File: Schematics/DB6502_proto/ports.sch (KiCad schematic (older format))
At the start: 29 parts, among them J1 System Bus, J10 AVR-ISP-6, J2 Controls, J3 Debug UART, J4 I/O Bus, J5 USB_B, J6 Power, J7 Power, J8 Power, J9 Power, U9 FT230XS

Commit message: Initial PCB layout
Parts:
- removed J6, J7, J8, J9: Power, symbol Connector:Conn_01x02_Female
- C13, C14, C15, C16: footprint (none) -> Capacitor_THT:C_Disc_D5.0mm_W2.5mm_P2.50mm
- D1, D2: footprint (none) -> LED_THT:LED_D3.0mm
- FB1, R1, R10, R11, R2, R3, R4, R5, R6, R7, R8, R9: footprint (none) -> Resistor_THT:R_Axial_DIN0207_L6.3mm_D2.5mm_P10.16mm_Horizontal
- J1, J2, J4: footprint (none) -> Connector_PinSocket_2.54mm:PinSocket_1x32_P2.54mm_Vertical
- J10: footprint (none) -> Connector_PinSocket_2.54mm:PinSocket_2x03_P2.54mm_Vertical
- J3: footprint (none) -> Connector_PinHeader_2.54mm:PinHeader_1x06_P2.54mm_Horizontal
- J5: footprint (none) -> Connector_USB:USB_B_OST_USB-B1HSxx_Horizontal
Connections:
- wire segments 231 -> 223
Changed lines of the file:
@@
 F 0 "J1" H 4728 6176 50  0000 L CNN
 F 1 "System Bus" H 4728 6085 50  0000 L CNN
-F 2 "" H 4700 6200 50  0001 C CNN
+F 2 "Connector_PinSocket_2.54mm:PinSocket_1x32_P2.54mm_Vertical" H 4700 6200 50  0001 C CNN
 F 3 "~" H 4700 6200 50  0001 C CNN
 	1    4700 6200
@@
 F 0 "R6" H 2230 1154 50  0000 R CNN
 F 1 "4K7" H 2230 1245 50  0000 R CNN
-F 2 "" V 2230 1200 50  0001 C CNN
+F 2 "Resistor_THT:R_Axial_DIN0207_L6.3mm_D2.5mm_P10.16mm_Horizontal" V 2230 1200 50  0001 C CNN
 F 3 "~" H 2300 1200 50  0001 C CNN
 	1    2300 1200
@@
 F 0 "R5" H 2070 1246 50  0000 L CNN
 F 1 "4K7" H 2070 1155 50  0000 L CNN
-F 2 "" V 1930 1200 50  0001 C CNN
+F 2 "Resistor_THT:R_Axial_DIN0207_L6.3mm_D2.5mm_P10.16mm_Horizontal" V 1930 1200 50  0001 C CNN
 F 3 "~" H 2000 1200 50  0001 C CNN
 	1    2000 1200
@@
 F 0 "R4" H 1770 1246 50  0000 L CNN
 F 1 "4K7" H 1770 1155 50  0000 L CNN
-F 2 "" V 1630 1200 50  0001 C CNN
+F 2 "Resistor_THT:R_Axial_DIN0207_L6.3mm_D2.5mm_P10.16mm_Horizontal" V 1630 1200 50  0001 C CNN
 F 3 "~" H 1700 1200 50  0001 C CNN
 	1    1700 1200
@@
 F 0 "R3" H 1470 1246 50  0000 L CNN
 F 1 "4K7" H 1470 1155 50  0000 L CNN
-F 2 "" V 1330 1200 50  0001 C CNN
+F 2 "Resistor_THT:R_Axial_DIN0207_L6.3mm_D2.5mm_P10.16mm_Horizontal" V 1330 1200 50  0001 C CNN
 F 3 "~" H 1400 1200 50  0001 C CNN
 	1    1400 1200
@@
 F 0 "R2" H 1170 1246 50  0000 L CNN
 F 1 "4K7" H 1170 1155 50  0000 L CNN
-F 2 "" V 1030 1200 50  0001 C CNN
+F 2 "Resistor_THT:R_Axial_DIN0207_L6.3mm_D2.5mm_P10.16mm_Horizontal" V 1030 1200 50  0001 C CNN
 F 3 "~" H 1100 1200 50  0001 C CNN
 	1    1100 1200
@@
 F 0 "J2" H 5178 2626 50  0000 L CNN
 F 1 "Controls" H 5178 2535 50  0000 L CNN
-F 2 "" H 5150 2650 50  0001 C CNN
+F 2 "Connector_PinSocket_2.54mm:PinSocket_1x32_P2.54mm_Vertical" H 5150 2650 50  0001 C CNN
 F 3 "~" H 5150 2650 50  0001 C CNN
 	1    5150 2650
@@
 F 0 "R1" H 870 1246 50  0000 L CNN
 F 1 "4K7" H 870 1155 50  0000 L CNN
-F 2 "" V 730 1200 50  0001 C CNN
+F 2 "Resistor_THT:R_Axial_DIN0207_L6.3mm_D2.5mm_P10.16mm_Horizontal" V 730 1200 50  0001 C CNN
 F 3 "~" H 800 1200 50  0001 C CNN
 	1    800  1200
@@
 F 0 "J4" H 8128 2576 50  0000 L CNN
 F 1 "I/O Bus" H 8128 2485 50  0000 L CNN
-F 2 "" H 8100 2600 50  0001 C CNN
+F 2 "Connector_PinSocket_2.54mm:PinSocket_1x32_P2.54mm_Vertical" H 8100 2600 50  0001 C CNN
 F 3 "~" H 8100 2600 50  0001 C CNN
 	1    8100 2600
@@
 F 0 "J10" H 10021 1696 50  0000 R CNN
 F 1 "AVR-ISP-6" H 10021 1605 50  0000 R CNN
-F 2 "" V 10100 1650 50  0001 C CNN
+F 2 "Connector_PinSocket_2.54mm:PinSocket_2x03_P2.54mm_Vertical" V 10100 1650 50  0001 C CNN
 F 3 " ~" H 9075 1050 50  0001 C CNN
 	1    10350 1600
@@
 F 0 "J5" H 9007 3467 50  0000 C CNN
 F 1 "USB_B" H 9007 3376 50  0000 C CNN
-F 2 "" H 9100 2950 50  0001 C CNN
+F 2 "Connector_USB:USB_B_OST_USB-B1HSxx_Horizontal" H 9100 2950 50  0001 C CNN
 F 3 "" H 9100 2950 50  0001 C CNN
 	1    8950 3000
@@
 F 0 "FB1" V 9563 2800 50  0000 C CNN
 F 1 "FB" V 9654 2800 50  0000 C CNN
-F 2 "" V 9730 2800 50  0001 C CNN
+F 2 "Resistor_THT:R_Axial_DIN0207_L6.3mm_D2.5mm_P10.16mm_Horizontal" V 9730 2800 50  0001 C CNN
 F 3 "~" H 9800 2800 50  0001 C CNN
 	1    9800 2800
@@
 F 0 "C15" H 9965 5496 50  0000 L CNN
 F 1 "100nF" H 9965 5405 50  0000 L CNN
-F 2 "" H 9888 5300 50  0001 C CNN
+F 2 "Capacitor_THT:C_Disc_D5.0mm_W2.5mm_P2.50mm" H 9888 5300 50  0001 C CNN
 F 3 "~" H 9850 5450 50  0001 C CNN
 	1    9850 5450
@@
 F 0 "R8" H 10370 5496 50  0000 L CNN
 F 1 "220" H 10370 5405 50  0000 L CNN
-F 2 "" V 10230 5450 50  0001 C CNN
+F 2 "Resistor_THT:R_Axial_DIN0207_L6.3mm_D2.5mm_P10.16mm_Horizontal" V 10230 5450 50  0001 C CNN
 F 3 "~" H 10300 5450 50  0001 C CNN
 	1    10300 5450
@@
 F 0 "R11" H 10670 5496 50  0000 L CNN
 F 1 "220" H 10670 5405 50  0000 L CNN
-F 2 "" V 10530 5450 50  0001 C CNN
+F 2 "Resistor_THT:R_Axial_DIN0207_L6.3mm_D2.5mm_P10.16mm_Horizontal" V 10530 5450 50  0001 C CNN
 F 3 "~" H 10600 5450 50  0001 C CNN
 	1    10600 5450
@@
 F 0 "D1" V 10339 5733 50  0000 R CNN
 F 1 "RX" V 10248 5733 50  0000 R CNN
-F 2 "" H 10300 5850 50  0001 C CNN
+F 2 "LED_THT:LED_D3.0mm" H 10300 5850 50  0001 C CNN
 F 3 "~" H 10300 5850 50  0001 C CNN
 	1    10300 5850
@@
 F 0 "D2" V 10639 5732 50  0000 R CNN
 F 1 "TX" V 10548 5732 50  0000 R CNN
-F 2 "" H 10600 5850 50  0001 C CNN
+F 2 "LED_THT:LED_D3.0mm" H 10600 5850 50  0001 C CNN
 F 3 "~" H 10600 5850 50  0001 C CNN
 	1    10600 5850
@@
 Wire Wire Line
 	6050 3300 7900 3300
-$Comp
-L Connector:Conn_01x02_Female J6
-U 1 1 6034CE9D
-P 9250 5400
-F 0 "J6" H 9278 5376 50  0000 L CNN
-F 1 "Power" H 9278 5285 50  0000 L CNN
-F 2 "" H 9250 5400 50  0001 C CNN
-F 3 "~" H 9250 5400 50  0001 C CNN
-	1    9250 5400
-	1    0    0    -1
-$EndComp
-Text GLabel 8950 5400 0    50   Input ~ 0
-+5V
-Text GLabel 8950 5500 0    50   Input ~ 0
-GND
-Wire Wire Line
-	8950 5400 9050 5400
-Wire Wire Line
-	8950 5500 9050 5500
-$Comp
-L Connector:Conn_01x02_Female J7
-U 1 1 60363BED
-P 9250 5650
-F 0 "J7" H 9278 5626 50  0000 L CNN
-F 1 "Power" H 9278 5535 50  0000 L CNN
-F 2 "" H 9250 5650 50  0001 C CNN
-F 3 "~" H 9250 5650 50  0001 C CNN
-	1    9250 5650
-	1    0    0    -1
-$EndComp
-Text GLabel 8950 5650 0    50   Input ~ 0
-+5V
-Text GLabel 8950 5750 0    50   Input ~ 0
-GND
-Wire Wire Line
-	8950 5650 9050 5650
-Wire Wire Line
-	8950 5750 9050 5750
-$Comp
-L Connector:Conn_01x02_Female J8
-U 1 1 6036B691
-P 9250 5900
-F 0 "J8" H 9278 5876 50  0000 L CNN
-F 1 "Power" H 9278 5785 50  0000 L CNN
-F 2 "" H 9250 5900 50  0001 C CNN
-F 3 "~" H 9250 5900 50  0001 C CNN
-	1    9250 5900
-	1    0    0    -1
-$EndComp
-Text GLabel 8950 5900 0    50   Input ~ 0
-+5V
-Text GLabel 8950 6000 0    50   Input ~ 0
-GND
-Wire Wire Line
-	8950 5900 9050 5900
-Wire Wire Line
-	8950 6000 9050 6000
-$Comp
-L Connector:Conn_01x02_Female J9
-U 1 1 6036B69F
-P 9250 6150
-F 0 "J9" H 9278 6126 50  0000 L CNN
-F 1 "Power" H 9278 6035 50  0000 L CNN
-F 2 "" H 9250 6150 50  0001 C CNN
-F 3 "~" H 9250 6150 50  0001 C CNN
-	1    9250 6150
-	1    0    0    -1
-$EndComp
-Text GLabel 8950 6150 0    50   Input ~ 0
-+5V
-Text GLabel 8950 6250 0    50   Input ~ 0
-GND
-Wire Wire Line
-	8950 6150 9050 6150
-Wire Wire Line
-	8950 6250 9050 6250
 Text GLabel 10750 3000 2    50   BiDi ~ 0
 USBD-
@@
 F 0 "R10" V 10600 3250 50  0000 C CNN
 F 1 "27" V 10500 3250 50  0000 C CNN
-F 2 "" V 10430 3250 50  0001 C CNN
+F 2 "Resistor_THT:R_Axial_DIN0207_L6.3mm_D2.5mm_P10.16mm_Horizontal" V 10430 3250 50  0001 C CNN
 F 3 "~" H 10500 3250 50  0001 C CNN
 	1    10500 3250
@@
 F 0 "R9" V 10600 3000 50  0000 C CNN
 F 1 "27" V 10500 3000 50  0000 C CNN
-F 2 "" V 10430 3000 50  0001 C CNN
+F 2 "Resistor_THT:R_Axial_DIN0207_L6.3mm_D2.5mm_P10.16mm_Horizontal" V 10430 3000 50  0001 C CNN
 F 3 "~" H 10500 3000 50  0001 C CNN
 	1    10500 3000
@@
 F 0 "C14" H 9892 3496 50  0000 L CNN
 F 1 "47pF" H 9892 3405 50  0000 L CNN
-F 2 "" H 9800 3450 50  0001 C CNN
+F 2 "Capacitor_THT:C_Disc_D5.0mm_W2.5mm_P2.50mm" H 9800 3450 50  0001 C CNN
 F 3 "~" H 9800 3450 50  0001 C CNN
 	1    9800 3450
@@
 F 0 "C16" H 10242 3496 50  0000 L CNN
 F 1 "47pF" H 10242 3405 50  0000 L CNN
-F 2 "" H 10150 3450 50  0001 C CNN
+F 2 "Capacitor_THT:C_Disc_D5.0mm_W2.5mm_P2.50mm" H 10150 3450 50  0001 C CNN
 F 3 "~" H 10150 3450 50  0001 C CNN
 	1    10150 3450
@@
 F 0 "C13" H 9542 3496 50  0000 L CNN
 F 1 "10nF" H 9542 3405 50  0000 L CNN
-F 2 "" H 9450 3450 50  0001 C CNN
+F 2 "Capacitor_THT:C_Disc_D5.0mm_W2.5mm_P2.50mm" H 9450 3450 50  0001 C CNN
 F 3 "~" H 9450 3450 50  0001 C CNN
 	1    9450 3450
@@
 F 0 "R7" H 2230 2554 50  0000 R CNN
 F 1 "4K7" H 2230 2645 50  0000 R CNN
-F 2 "" V 2230 2600 50  0001 C CNN
+F 2 "Resistor_THT:R_Axial_DIN0207_L6.3mm_D2.5mm_P10.16mm_Horizontal" V 2230 2600 50  0001 C CNN
 F 3 "~" H 2300 2600 50  0001 C CNN
 	1    2300 2600
@@
 F 0 "J3" H 7958 5231 50  0000 C CNN
 F 1 "Debug UART" H 7958 5140 50  0000 C CNN
-F 2 "" H 7850 4850 50  0001 C CNN
+F 2 "Connector_PinHeader_2.54mm:PinHeader_1x06_P2.54mm_Horizontal" H 7850 4850 50  0001 C CNN
 F 3 "~" H 7850 4850 50  0001 C CNN
 	1    7850 4850
@@
 Wire Wire Line
 	8950 3600 8950 3500
+Connection ~ 8950 3500
 Wire Bus Line
 	11000 1300 11000 1500
@@
 Wire Bus Line
 	3100 6700 4600 6700
-Connection ~ 8950 3500
 $EndSCHEMATC

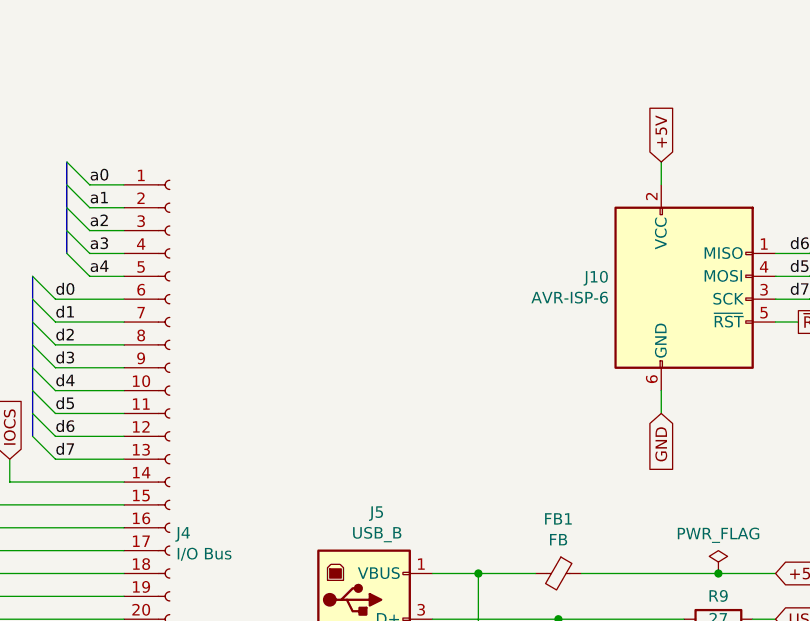
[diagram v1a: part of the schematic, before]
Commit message: Ordered DB6502 proto PCB
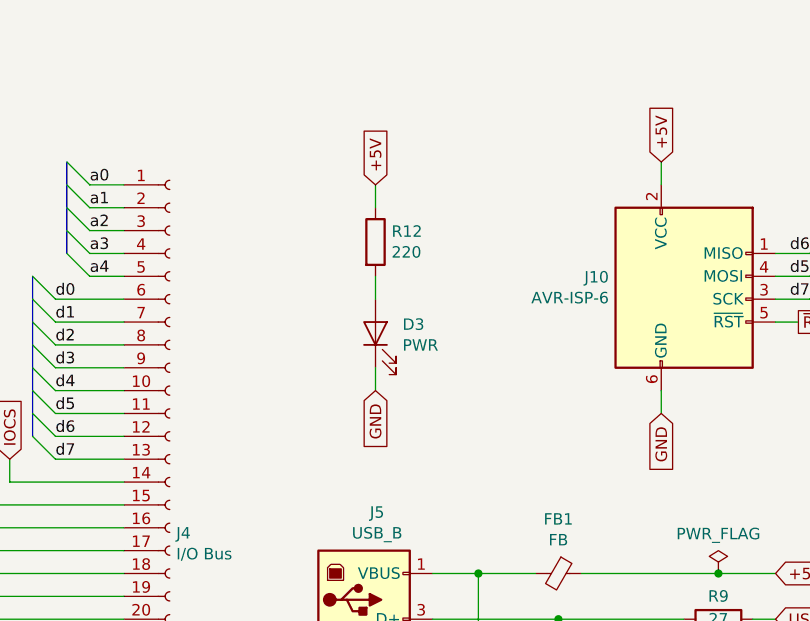
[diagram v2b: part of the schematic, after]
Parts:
- added D3: PWR, LED_THT:LED_D3.0mm, symbol Device:LED
- added R12: 220, Resistor_THT:R_Axial_DIN0207_L6.3mm_D2.5mm_P10.16mm_Horizontal, symbol Device:R
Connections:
- net +5V: now also R12.1
- net GND: now also D3.1 (K)
- new net: D3.2 (A), R12.2
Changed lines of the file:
@@
 	8950 3600 8950 3500
 Connection ~ 8950 3500
+$Comp
+L Device:R R12
+U 1 1 60B17A68
+P 9000 1350
+F 0 "R12" H 9070 1396 50  0000 L CNN
+F 1 "220" H 9070 1305 50  0000 L CNN
+F 2 "Resistor_THT:R_Axial_DIN0207_L6.3mm_D2.5mm_P10.16mm_Horizontal" V 8930 1350 50  0001 C CNN
+F 3 "~" H 9000 1350 50  0001 C CNN
+	1    9000 1350
+	1    0    0    -1
+$EndComp
+$Comp
+L Device:LED D3
+U 1 1 60B19002
+P 9000 1750
+F 0 "D3" V 9039 1632 50  0000 R CNN
+F 1 "PWR" V 8948 1632 50  0000 R CNN
+F 2 "LED_THT:LED_D3.0mm" H 9000 1750 50  0001 C CNN
+F 3 "~" H 9000 1750 50  0001 C CNN
+	1    9000 1750
+	0    -1   -1   0
+$EndComp
+Text GLabel 9000 1100 1    50   Input ~ 0
++5V
+Wire Wire Line
+	9000 1100 9000 1200
+Wire Wire Line
+	9000 1500 9000 1600
+Text GLabel 9000 2000 3    50   Input ~ 0
+GND
+Wire Wire Line
+	9000 2000 9000 1900
 Wire Bus Line
 	11000 1300 11000 1500

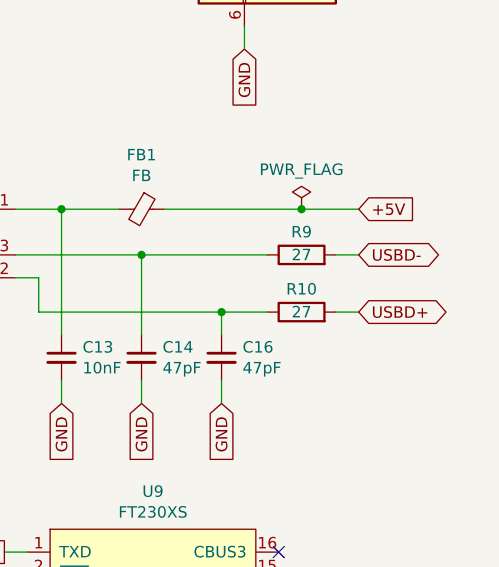
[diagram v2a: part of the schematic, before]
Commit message: Fixed bug with D+/D- switched
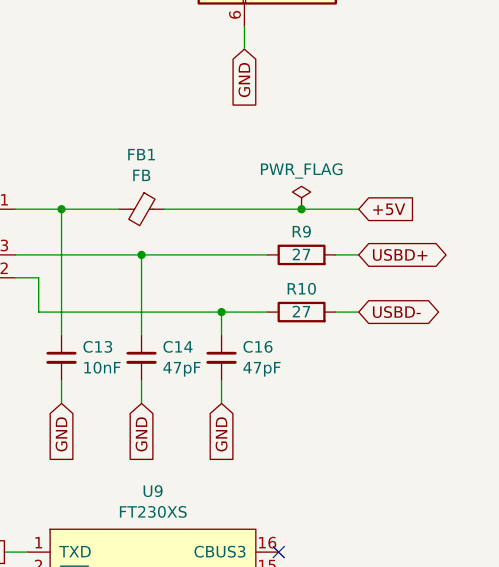
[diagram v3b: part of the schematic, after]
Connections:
- net USBD+: now also R9.2; no longer R10.2
- net USBD-: now also R10.2; no longer R9.2
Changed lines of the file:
@@
 Wire Wire Line
 	6050 3300 7900 3300
+Text GLabel 10750 3250 2    50   BiDi ~ 0
+USBD-
 Text GLabel 10750 3000 2    50   BiDi ~ 0
-USBD-
-Text GLabel 10750 3250 2    50   BiDi ~ 0
 USBD+
 $Comp

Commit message: Last missing fix for the AVR ISP - footprint association.
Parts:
- J10: footprint Connector_PinSocket_2.54mm:PinSocket_2x03_P2.54mm_Vertical -> Connector_PinHeader_2.54mm:PinHeader_2x03_P2.54mm_Vertical
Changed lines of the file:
@@
 F 0 "J10" H 10021 1696 50  0000 R CNN
 F 1 "AVR-ISP-6" H 10021 1605 50  0000 R CNN
-F 2 "Connector_PinSocket_2.54mm:PinSocket_2x03_P2.54mm_Vertical" V 10100 1650 50  0001 C CNN
+F 2 "Connector_PinHeader_2.54mm:PinHeader_2x03_P2.54mm_Vertical" V 10100 1650 50  0001 C CNN
 F 3 " ~" H 9075 1050 50  0001 C CNN
 	1    10350 1600

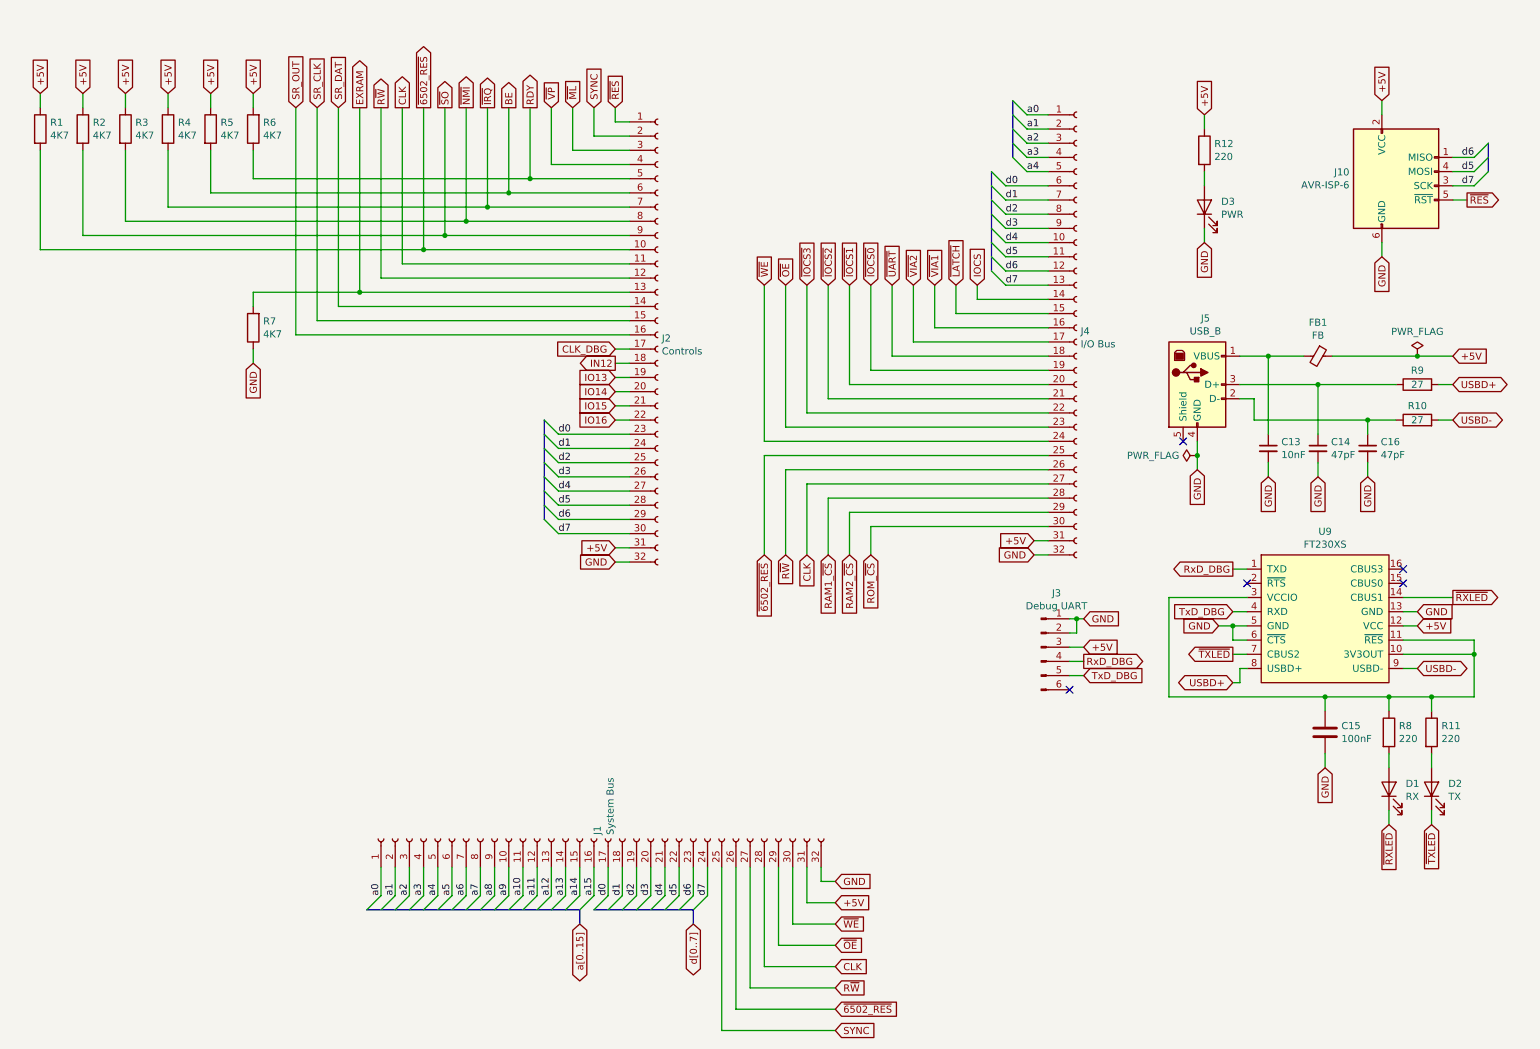
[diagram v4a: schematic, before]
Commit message: Started documenting current system layout
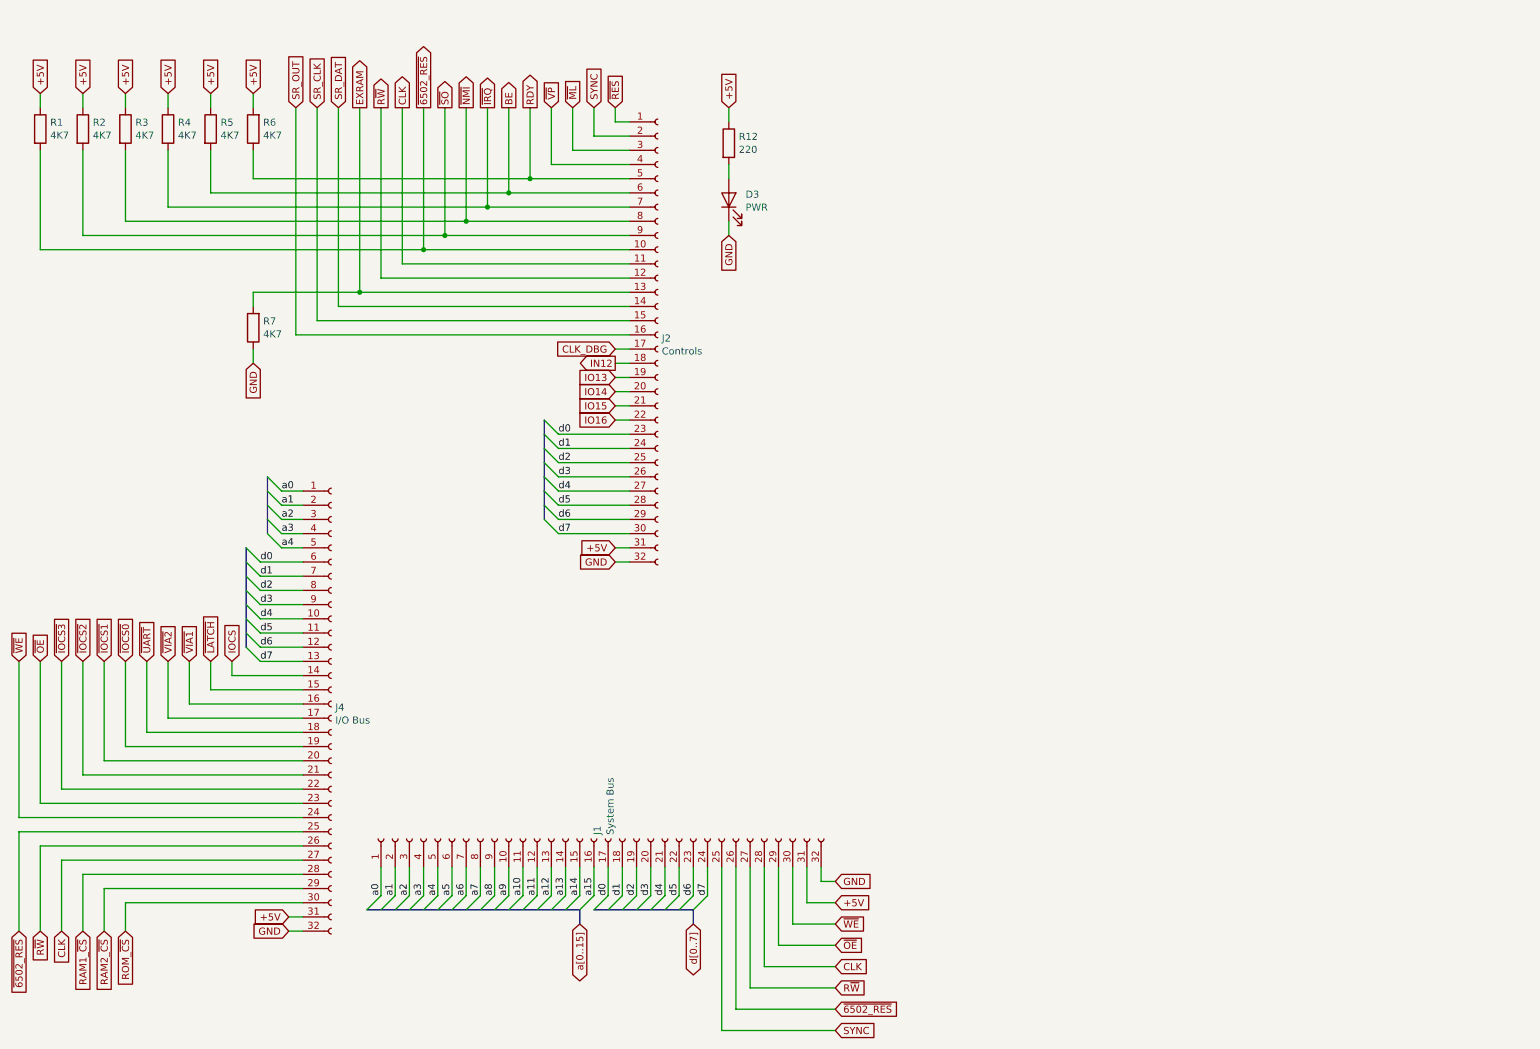
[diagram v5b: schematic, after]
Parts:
- removed C13: 10nF, Capacitor_THT:C_Disc_D5.0mm_W2.5mm_P2.50mm, symbol Device:C_Small
- removed C14, C16: 47pF, Capacitor_THT:C_Disc_D5.0mm_W2.5mm_P2.50mm, symbol Device:C_Small
- removed C15: 100nF, Capacitor_THT:C_Disc_D5.0mm_W2.5mm_P2.50mm, symbol Device:C
- removed D1: RX, LED_THT:LED_D3.0mm, symbol Device:LED
- removed D2: TX, LED_THT:LED_D3.0mm, symbol Device:LED
- removed FB1: FB, Resistor_THT:R_Axial_DIN0207_L6.3mm_D2.5mm_P10.16mm_Horizontal, symbol Device:Ferrite_Bead_Small
- removed J10: AVR-ISP-6, Connector_PinHeader_2.54mm:PinHeader_2x03_P2.54mm_Vertical, symbol Connector:AVR-ISP-6
- removed J3: Debug UART, Connector_PinHeader_2.54mm:PinHeader_1x06_P2.54mm_Horizontal, symbol Connector:Conn_01x06_Male
- removed J5: USB_B, Connector_USB:USB_B_OST_USB-B1HSxx_Horizontal, symbol 6502:USB_B
- removed R10, R9: 27, Resistor_THT:R_Axial_DIN0207_L6.3mm_D2.5mm_P10.16mm_Horizontal, symbol Device:R
- removed R11, R8: 220, Resistor_THT:R_Axial_DIN0207_L6.3mm_D2.5mm_P10.16mm_Horizontal, symbol Device:R
- removed U9: FT230XS, Package_SO:SSOP-16_5.3x6.2mm_P0.65mm, symbol 6502:FT230XS
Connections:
- no-connect marks 5 -> 0
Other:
- moved on the sheet: D3, J4, R12
